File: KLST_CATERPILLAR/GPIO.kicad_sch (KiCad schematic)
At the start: 1 part, among them J13 GPIO

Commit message: reduced modules
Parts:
- added J2, J3: GPIO, Connector_IDC:IDC-Header_2x17_P2.54mm_Horizontal, symbol Connector_Generic:Conn_02x17_Odd_Even
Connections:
- net +3.3V: now also J2.1 (Pin_1), J3.1 (Pin_1)
- net +5V: now also J2.2 (Pin_2), J3.2 (Pin_2)
- net GND: now also J2.33 (Pin_33), J2.34 (Pin_34), J2.4 (Pin_4), J3.33 (Pin_33), J3.34 (Pin_34), J3.4 (Pin_4); no longer J13.24 (Pin_24), J13.3 (Pin_3)
- new net +1.8V: J13.3 (Pin_3), J2.3 (Pin_3), J3.3 (Pin_3)
- new net _ADC_USR: J2.16 (Pin_16)
- new net _BUTTON_PROGRAMMER: J13.24 (Pin_24)
- new net _DAC_USR: J2.14 (Pin_14)
- new net _DISPLAY_BACKLIGHT_PWM: J2.27 (Pin_27)
- new net _DISPLAY_LTDC_B0: J3.10 (Pin_10)
- new net _DISPLAY_LTDC_B1: J3.12 (Pin_12)
- new net _DISPLAY_LTDC_B2: J3.14 (Pin_14)
- new net _DISPLAY_LTDC_B3: J3.16 (Pin_16)
- new net _DISPLAY_LTDC_B4: J3.18 (Pin_18)
- new net _DISPLAY_LTDC_B5: J3.20 (Pin_20)
- new net _DISPLAY_LTDC_B6: J3.22 (Pin_22)
- new net _DISPLAY_LTDC_B7: J3.24 (Pin_24)
- new net _DISPLAY_LTDC_CLK: J3.26 (Pin_26)
- new net _DISPLAY_LTDC_DE: J3.28 (Pin_28)
- new net _DISPLAY_LTDC_G0: J3.21 (Pin_21)
- new net _DISPLAY_LTDC_G1: J3.23 (Pin_23)
- new net _DISPLAY_LTDC_G2: J3.25 (Pin_25)
- new net _DISPLAY_LTDC_G3: J3.27 (Pin_27)
- new net _DISPLAY_LTDC_G4: J3.29 (Pin_29)
- new net _DISPLAY_LTDC_G5: J3.31 (Pin_31)
- new net _DISPLAY_LTDC_G6: J3.6 (Pin_6)
- new net _DISPLAY_LTDC_G7: J3.8 (Pin_8)
- new net _DISPLAY_LTDC_HSYNC: J3.32 (Pin_32)
- new net _DISPLAY_LTDC_R0: J3.5 (Pin_5)
- new net _DISPLAY_LTDC_R1: J3.7 (Pin_7)
- new net _DISPLAY_LTDC_R2: J3.9 (Pin_9)
- new net _DISPLAY_LTDC_R3: J3.11 (Pin_11)
- new net _DISPLAY_LTDC_R4: J3.13 (Pin_13)
- new net _DISPLAY_LTDC_R5: J3.15 (Pin_15)
- new net _DISPLAY_LTDC_R6: J3.17 (Pin_17)
- new net _DISPLAY_LTDC_R7: J3.19 (Pin_19)
- new net _DISPLAY_LTDC_VSYNC: J3.30 (Pin_30)
- new net _DISPLAY_ON_OFF: J2.31 (Pin_31)
- new net _DISPLAY_TOUCH_INTERRUPT: J2.29 (Pin_29)
- new net _ENCODER_00_A: J2.5 (Pin_5)
- new net _ENCODER_00_B: J2.7 (Pin_7)
- new net _ENCODER_00_BUTTON: J2.9 (Pin_9)
- new net _ENCODER_01_A: J2.6 (Pin_6)
- new net _ENCODER_01_B: J2.8 (Pin_8)
- new net _ENCODER_01_BUTTON: J2.11 (Pin_11)
- new net _EXT_MEMORY_A0: J2.24 (Pin_24)
- new net _EXT_MEMORY_A1: J2.26 (Pin_26)
- new net _EXT_MEMORY_A2: J2.28 (Pin_28)
- new net _EXT_MEMORY_A3: J2.30 (Pin_30)
- new net _EXT_MEMORY_A4: J2.32 (Pin_32)
- new net _EXT_MEMORY_A5: J2.21 (Pin_21)
- new net _EXT_MEMORY_A6: J2.23 (Pin_23)
- new net _EXT_MEMORY_A7: J2.25 (Pin_25)
- new net _EXT_MEMORY_CHIP_SELECT: J2.22 (Pin_22)
- new net _EXT_MEMORY_CLK: J2.20 (Pin_20)
- new net _EXT_MEMORY_DQS: J2.18 (Pin_18)
- new net _IDC_SERIAL_01_RX: J2.13 (Pin_13)
- new net _IDC_SERIAL_01_TX: J2.15 (Pin_15)
- new net _MECH_BUTTON_00: J2.17 (Pin_17)
- new net _MECH_BUTTON_01: J2.19 (Pin_19)
- new net _MIDI_ANALOG_IN: J2.12 (Pin_12)
- new net _MIDI_ANALOG_OUT: J2.10 (Pin_10)
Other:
- note added: "GPIO ( unused modules #1 )"
- note added: "GPIO ( unused modules #2 )"

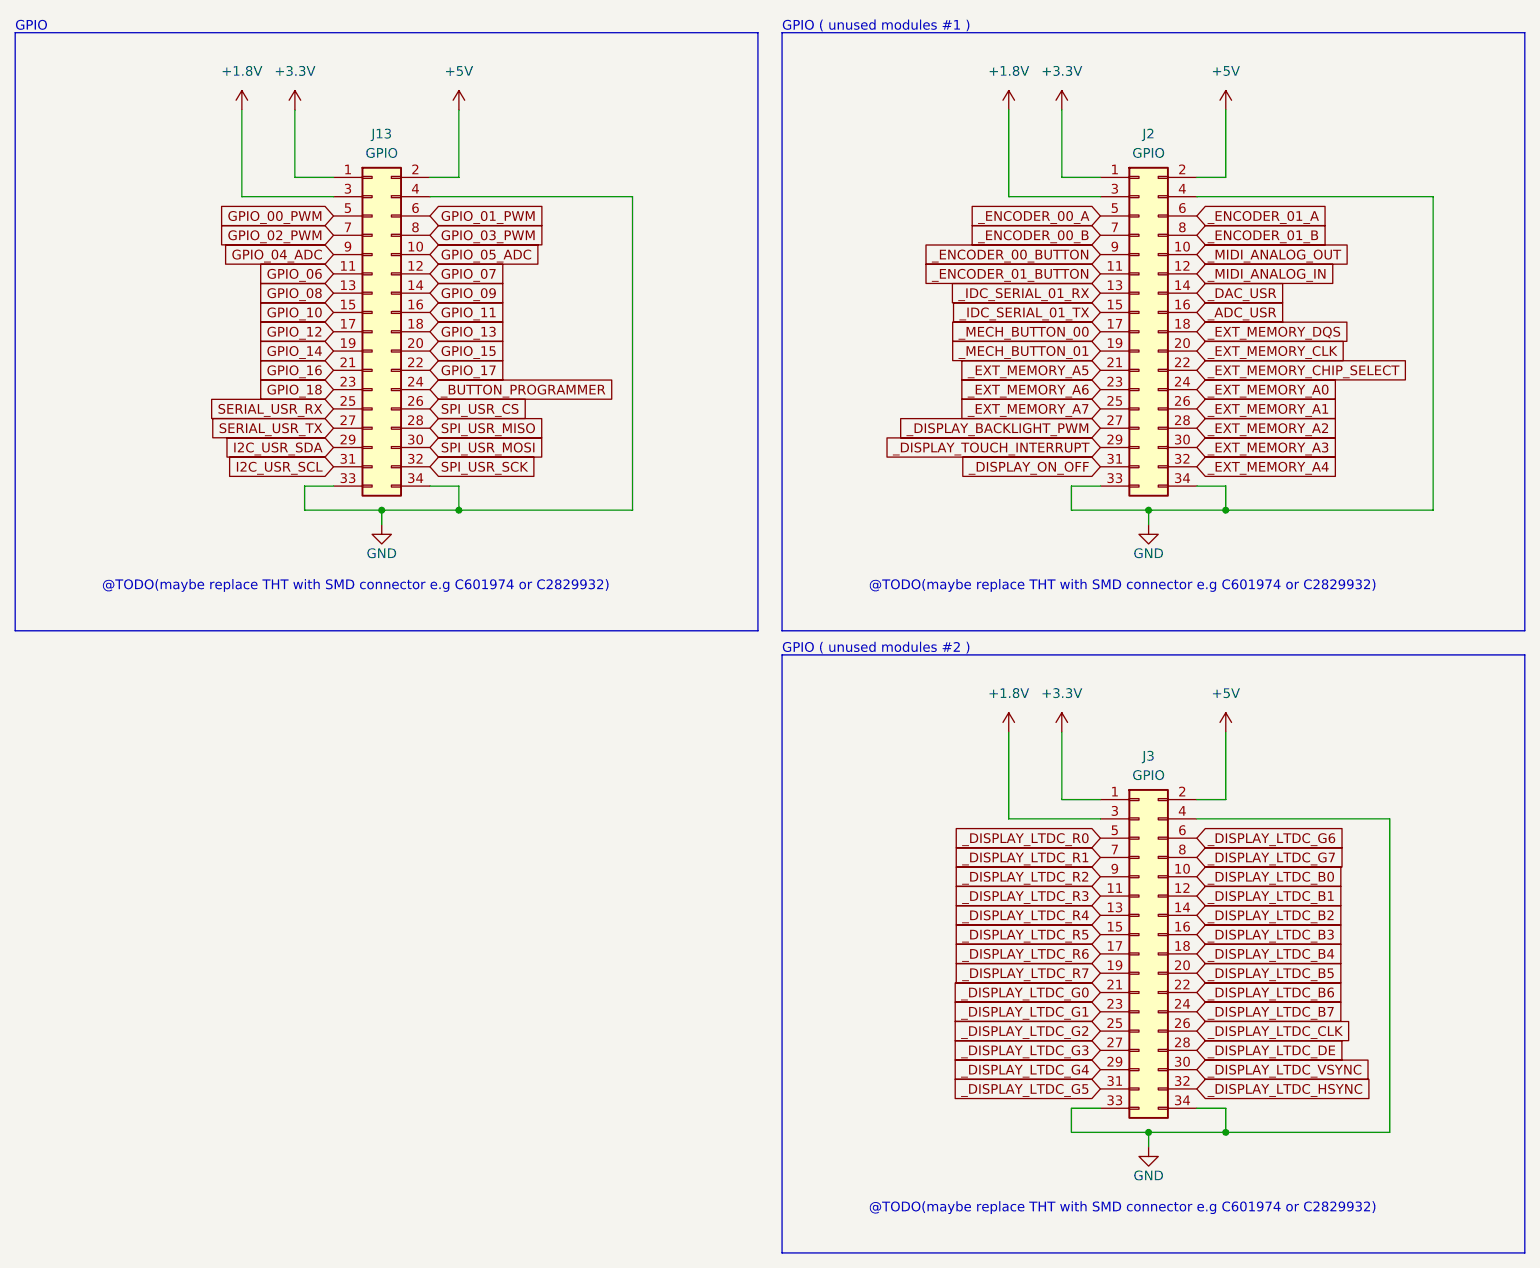
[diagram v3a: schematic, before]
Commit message: added GPIOs
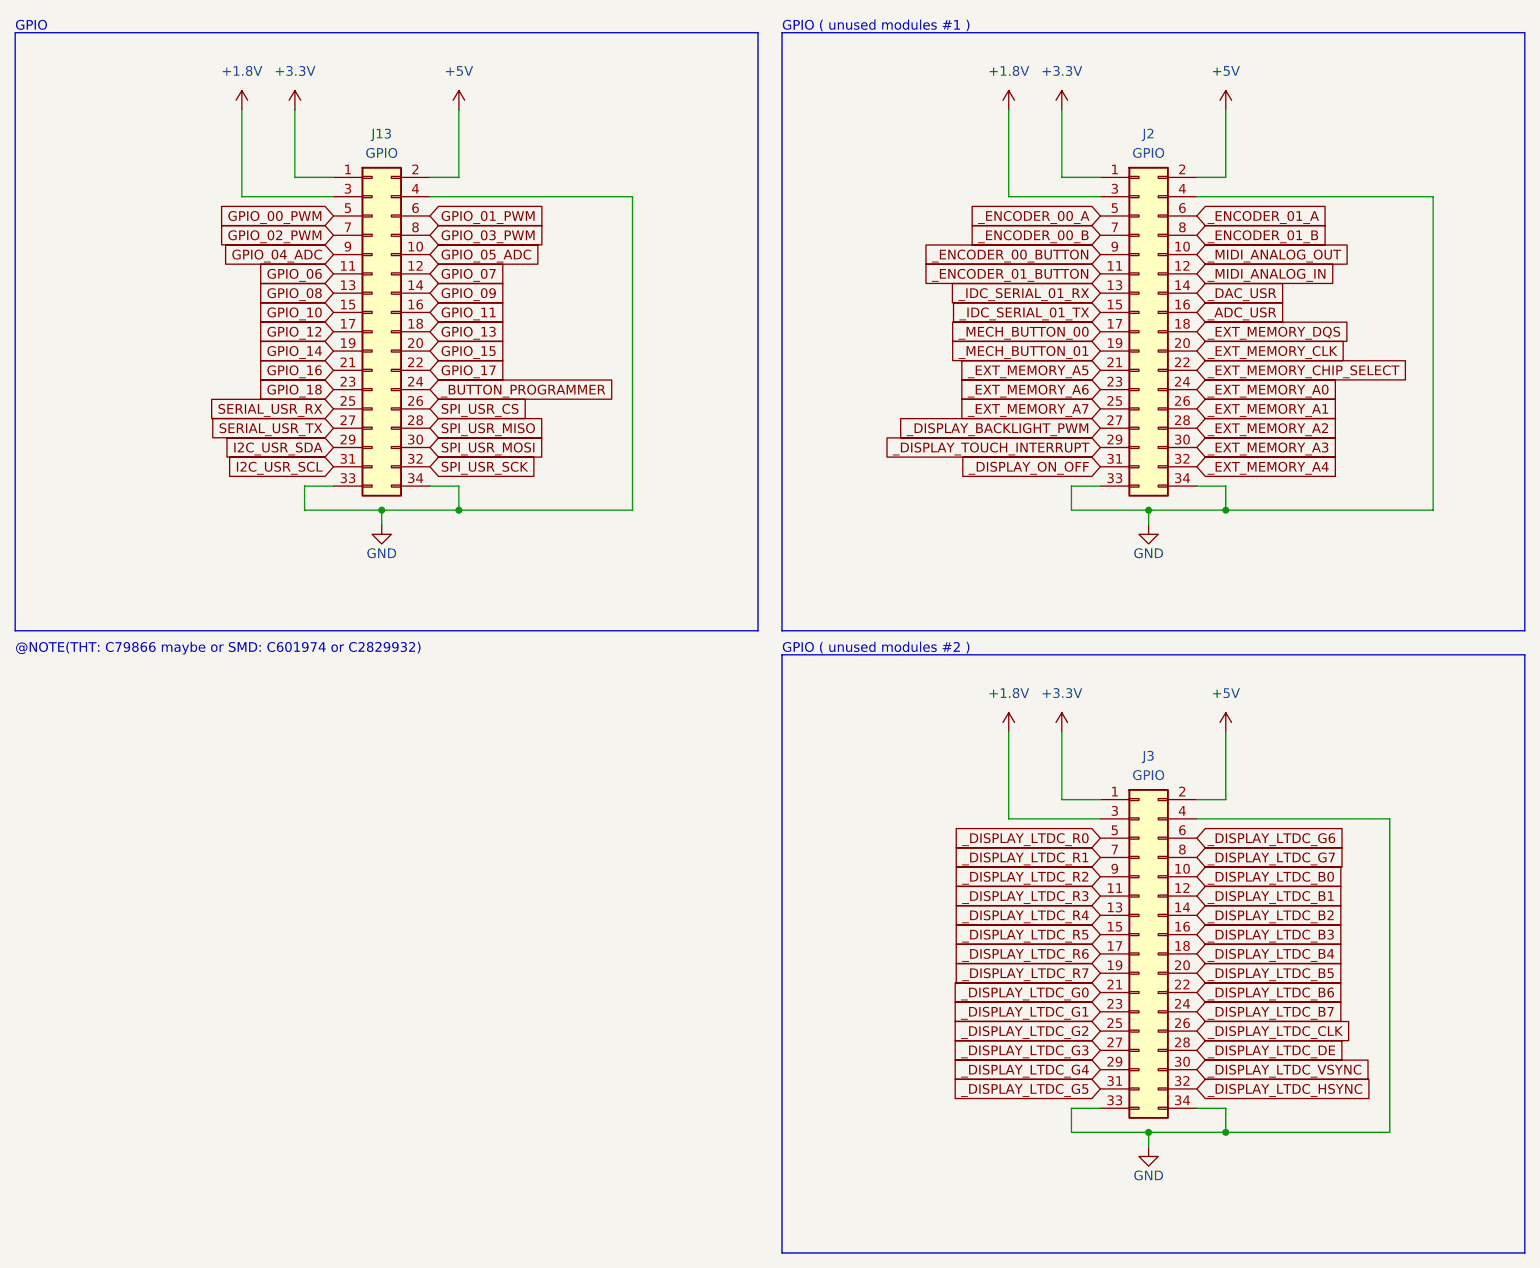
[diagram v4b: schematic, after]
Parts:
- J13: footprint Connector_IDC:IDC-Header_2x17_P2.54mm_Horizontal -> IDC-connector_SMD:IDC-PinHeader_2x17_P2.54mm_Vertical_SMD; JLCPCB C79866 -> C2829932
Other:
- note added: "@NOTE(THT: C79866 maybe or SMD: C601974 or C2829932)"
- note removed: "@TODO(maybe replace THT with SMD connector e.g C601974 or C2829932)"
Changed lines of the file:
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@@
 		)
 	)
-	(text "@TODO(maybe replace THT with SMD connector e.g C601974 or C2829932)"
+	(text "@NOTE(THT: C79866 maybe or SMD: C601974 or C2829932)"
 		(exclude_from_sim no)
-		(at 26.67 88.9 0)
+		(at 15.24 97.155 0)
 		(effects
 			(font
@@
 		(exclude_from_sim no)
 		(at 116.205 97.155 0)
-		(effects
-			(font
-				(size 1.27 1.27)
-			)
-			(justify left bottom)
-		)
-	)
-	(text "@TODO(maybe replace THT with SMD connector e.g C601974 or C2829932)"
-		(exclude_from_sim no)
-		(at 127.635 88.9 0)
-		(effects
-			(font
-				(size 1.27 1.27)
-			)
-			(justify left bottom)
-		)
-	)
-	(text "@TODO(maybe replace THT with SMD connector e.g C601974 or C2829932)"
-		(exclude_from_sim no)
-		(at 127.635 170.815 0)
 		(effects
 			(font
@@
 		(exclude_from_sim no)
 		(in_bom yes)
-		(on_board no)
+		(on_board yes)
 		(dnp no)
 		(fields_autoplaced yes)
@@
 			)
 		)
-		(property "Footprint" "Connector_IDC:IDC-Header_2x17_P2.54mm_Horizontal"
+		(property "Footprint" "IDC-connector_SMD:IDC-PinHeader_2x17_P2.54mm_Vertical_SMD"
 			(at 62.23 54.61 0)
 			(effects
@@
 			)
 		)
-		(property "JLCPCB" "C79866"
+		(property "JLCPCB" "C2829932"
 			(at 62.23 54.61 0)
 			(effects

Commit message: added test points, replaced unavailable components
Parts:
- J13: now not fitted
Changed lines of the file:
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@@
 		(in_bom yes)
 		(on_board yes)
-		(dnp no)
+		(dnp yes)
 		(fields_autoplaced yes)
 		(property "Reference" "J13"
